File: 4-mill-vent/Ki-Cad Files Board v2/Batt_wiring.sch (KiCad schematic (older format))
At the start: 4 parts, among them J10 Fan, J13 buzzer, M1 Fan_4pin

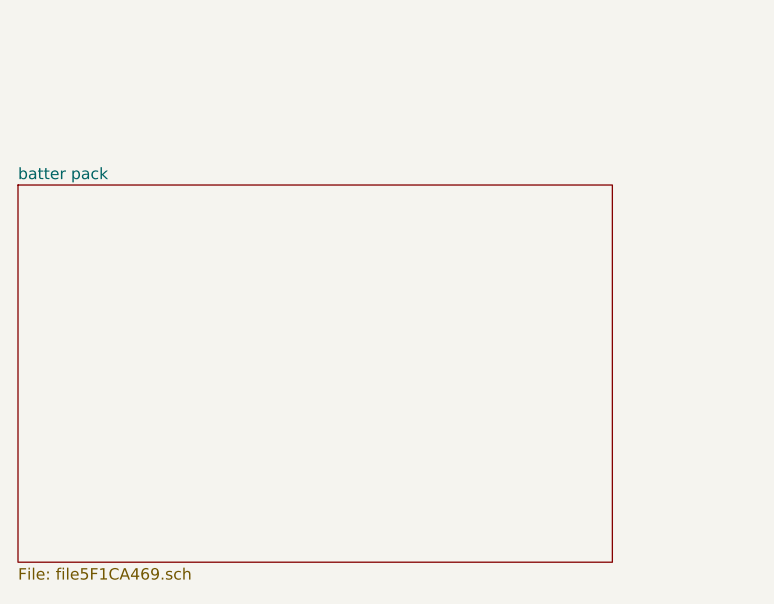
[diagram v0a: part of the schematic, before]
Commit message: Last Update USE V2
Board test complete, all slikscreen error are fixed in v2, Full use of opamp for battery monitoring.
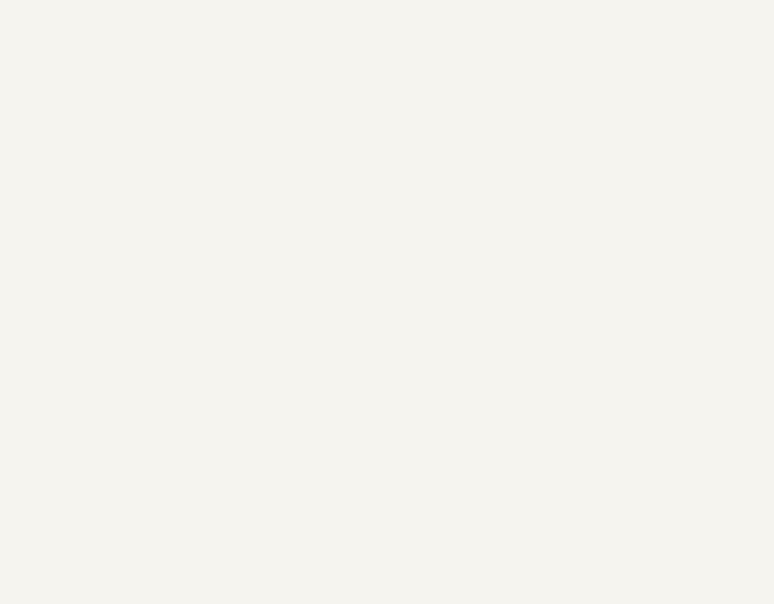
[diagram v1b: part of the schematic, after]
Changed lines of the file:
@@
 $Descr A4 11693 8268
 encoding utf-8
-Sheet 2 4
+Sheet 2 2
 Title ""
 Date ""
@@
 	-1   0    0    1
 $EndComp
-$Sheet
-S 3050 5350 2600 1650
-U 5F1CA46A
-F0 "batter pack" 50
-F1 "file5F1CA469.sch" 50
-$EndSheet
 $Comp
 L Motor:Fan_4pin M1
